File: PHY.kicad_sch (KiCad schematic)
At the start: 29 parts, among them U13 LAN8742A, Y3 25Mhz

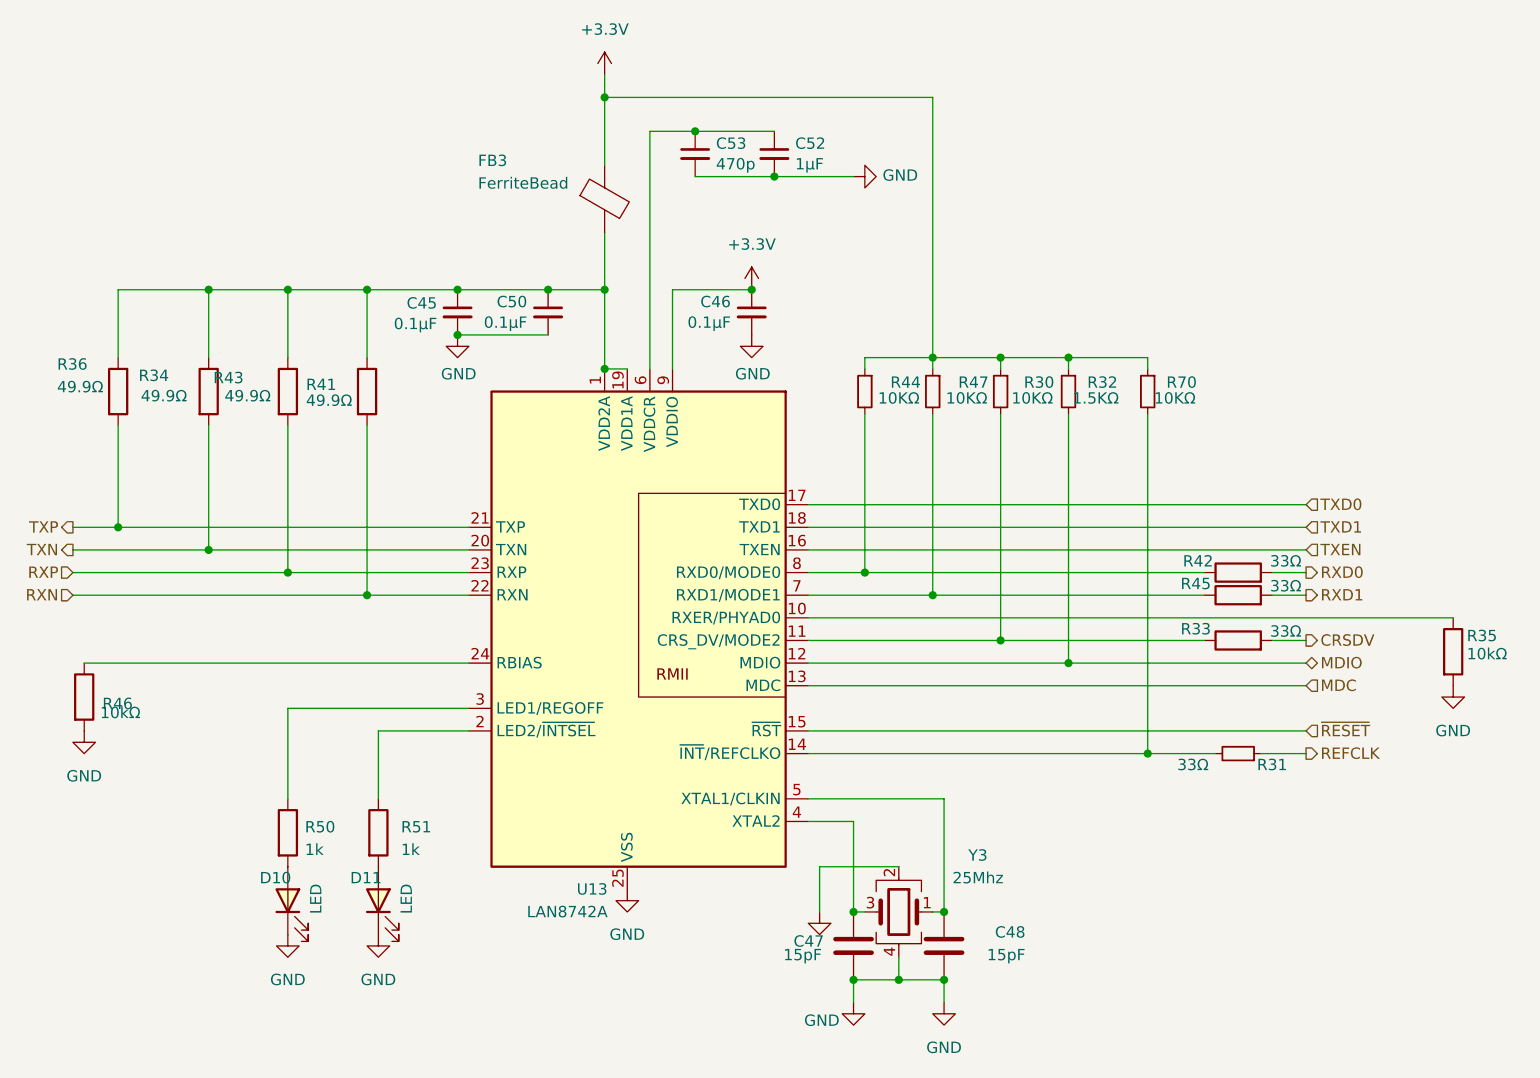
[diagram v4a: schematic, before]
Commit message: add sata capacitor
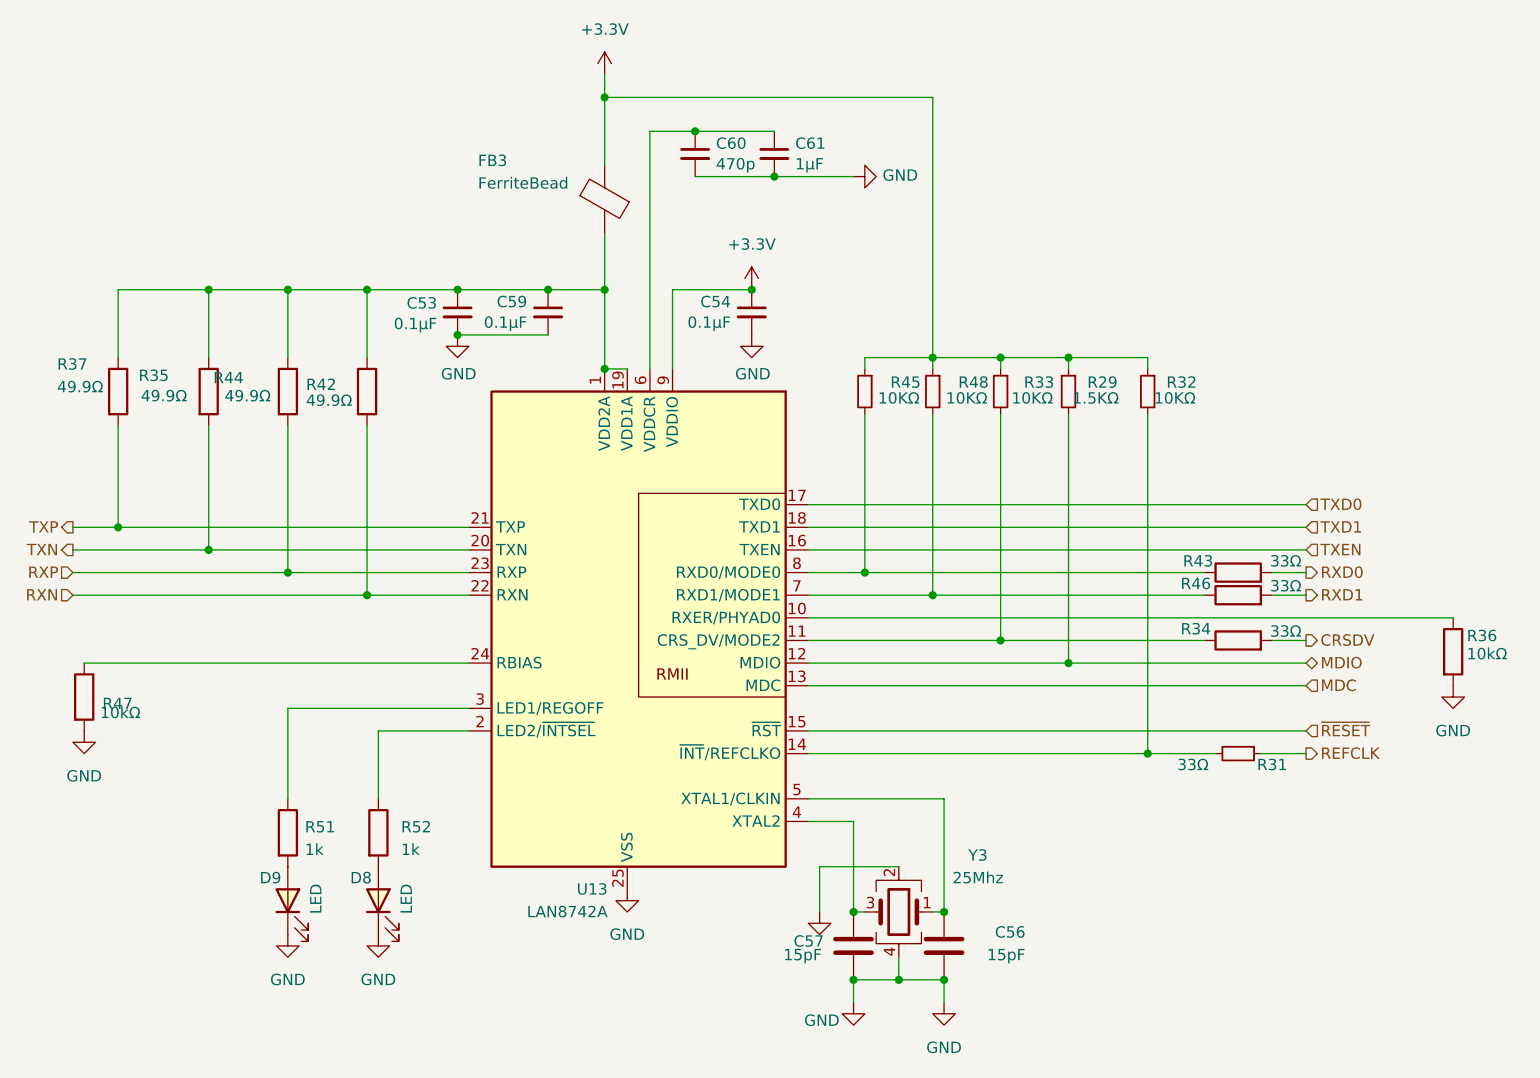
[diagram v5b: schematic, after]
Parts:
- renumbered C45 to C53, C46 to C54, C48 to C56, C47 to C57, C50 to C59, C53 to C60, C52 to C61, D11 to D8, D10 to D9, R32 to R29, R70 to R32, R30 to R33, R33 to R34, R34 to R35, R35 to R36, R36 to R37, R41 to R42, R42 to R43, R43 to R44, R44 to R45, R45 to R46, R46 to R47, R47 to R48, R50 to R51, R51 to R52
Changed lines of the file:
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@@
 		(shape input)
 		(at 78.74 116.84 180)
+		(fields_autoplaced yes)
 		(effects
 			(font
@@
 		(shape output)
 		(at 217.17 121.92 0)
+		(fields_autoplaced yes)
 		(effects
 			(font
@@
 		(shape output)
 		(at 78.74 109.22 180)
+		(fields_autoplaced yes)
 		(effects
 			(font
@@
 		(shape input)
 		(at 78.74 114.3 180)
+		(fields_autoplaced yes)
 		(effects
 			(font
@@
 		(shape output)
 		(at 217.17 134.62 0)
+		(fields_autoplaced yes)
 		(effects
 			(font
@@
 		(shape input)
 		(at 217.17 106.68 0)
+		(fields_autoplaced yes)
 		(effects
 			(font
@@
 		(shape output)
 		(at 217.17 116.84 0)
+		(fields_autoplaced yes)
 		(effects
 			(font
@@
 		(shape input)
 		(at 217.17 109.22 0)
+		(fields_autoplaced yes)
 		(effects
 			(font
@@
 		(shape input)
 		(at 217.17 127 0)
+		(fields_autoplaced yes)
 		(effects
 			(font
@@
 		(shape input)
 		(at 217.17 132.08 0)
+		(fields_autoplaced yes)
 		(effects
 			(font
@@
 		(shape output)
 		(at 217.17 114.3 0)
+		(fields_autoplaced yes)
 		(effects
 			(font
@@
 		(shape input)
 		(at 217.17 111.76 0)
+		(fields_autoplaced yes)
 		(effects
 			(font
@@
 		(shape bidirectional)
 		(at 217.17 124.46 0)
+		(fields_autoplaced yes)
 		(effects
 			(font
@@
 		(shape output)
 		(at 78.74 111.76 180)
+		(fields_autoplaced yes)
 		(effects
 			(font
@@
 		(on_board yes)
 		(dnp no)
-		(property "Reference" "R45"
+		(property "Reference" "R46"
 			(at 206.502 115.57 90)
 			(effects
@@
 			(project "mainboard4"
 				(path "/dd07ab80-a59c-44f4-ac7d-849e21e1384e/4fc6aed4-b6ec-46a7-b9d1-1f9060000df7"
-					(reference "R45")
+					(reference "R46")
 					(unit 1)
 				)
@@
 		(on_board yes)
 		(dnp no)
-		(property "Reference" "R43"
+		(property "Reference" "R44"
 			(at 94.488 92.456 0)
 			(effects
@@
 			(project "mainboard4"
 				(path "/dd07ab80-a59c-44f4-ac7d-849e21e1384e/4fc6aed4-b6ec-46a7-b9d1-1f9060000df7"
-					(reference "R43")
+					(reference "R44")
 					(unit 1)
 				)
@@
 		(on_board yes)
 		(dnp no)
-		(property "Reference" "C46"
+		(property "Reference" "C54"
 			(at 152.6032 83.9216 0)
 			(effects
@@
 			(project "mainboard4"
 				(path "/dd07ab80-a59c-44f4-ac7d-849e21e1384e/4fc6aed4-b6ec-46a7-b9d1-1f9060000df7"
-					(reference "C46")
+					(reference "C54")
 					(unit 1)
 				)
@@
 		(on_board yes)
 		(dnp no)
-		(property "Reference" "C50"
+		(property "Reference" "C59"
 			(at 129.7432 83.9216 0)
 			(effects
@@
 			(project "mainboard4"
 				(path "/dd07ab80-a59c-44f4-ac7d-849e21e1384e/4fc6aed4-b6ec-46a7-b9d1-1f9060000df7"
-					(reference "C50")
+					(reference "C59")
 					(unit 1)
 				)
@@
 		(on_board yes)
 		(dnp no)
-		(property "Reference" "D10"
+		(property "Reference" "D9"
 			(at 99.695 148.59 90)
 			(effects
@@
 			(project "mainboard4"
 				(path "/dd07ab80-a59c-44f4-ac7d-849e21e1384e/4fc6aed4-b6ec-46a7-b9d1-1f9060000df7"
-					(reference "D10")
+					(reference "D9")
 					(unit 1)
 				)
@@
 		(on_board yes)
 		(dnp no)
-		(property "Reference" "R46"
+		(property "Reference" "R47"
 			(at 82.042 129.032 0)
 			(effects
@@
 			(project "mainboard4"
 				(path "/dd07ab80-a59c-44f4-ac7d-849e21e1384e/4fc6aed4-b6ec-46a7-b9d1-1f9060000df7"
-					(reference "R46")
+					(reference "R47")
 					(unit 1)
 				)
@@
 		(on_board yes)
 		(dnp no)
-		(property "Reference" "R36"
+		(property "Reference" "R37"
 			(at 76.962 90.932 0)
 			(effects
@@
 			(project "mainboard4"
 				(path "/dd07ab80-a59c-44f4-ac7d-849e21e1384e/4fc6aed4-b6ec-46a7-b9d1-1f9060000df7"
-					(reference "R36")
+					(reference "R37")
 					(unit 1)
 				)
@@
 		(on_board yes)
 		(dnp no)
-		(property "Reference" "R42"
+		(property "Reference" "R43"
 			(at 206.756 113.03 90)
 			(effects
@@
 			(project "mainboard4"
 				(path "/dd07ab80-a59c-44f4-ac7d-849e21e1384e/4fc6aed4-b6ec-46a7-b9d1-1f9060000df7"
-					(reference "R42")
+					(reference "R43")
 					(unit 1)
 				)
@@
 		(on_board yes)
 		(dnp no)
-		(property "Reference" "R41"
+		(property "Reference" "R42"
 			(at 104.902 93.218 0)
 			(effects
@@
 			(project "mainboard4"
 				(path "/dd07ab80-a59c-44f4-ac7d-849e21e1384e/4fc6aed4-b6ec-46a7-b9d1-1f9060000df7"
-					(reference "R41")
+					(reference "R42")
 					(unit 1)
 				)
@@
 		(on_board yes)
 		(dnp no)
-		(property "Reference" "R35"
+		(property "Reference" "R36"
 			(at 235.204 121.412 0)
 			(effects
@@
 			(project "mainboard4"
 				(path "/dd07ab80-a59c-44f4-ac7d-849e21e1384e/4fc6aed4-b6ec-46a7-b9d1-1f9060000df7"
-					(reference "R35")
+					(reference "R36")
 					(unit 1)
 				)
@@
 		(on_board yes)
 		(dnp no)
-		(property "Reference" "R34"
+		(property "Reference" "R35"
 			(at 86.106 92.202 0)
 			(effects
@@
 			(project "mainboard4"
 				(path "/dd07ab80-a59c-44f4-ac7d-849e21e1384e/4fc6aed4-b6ec-46a7-b9d1-1f9060000df7"
-					(reference "R34")
+					(reference "R35")
 					(unit 1)
 				)
@@
 		(on_board yes)
 		(dnp no)
-		(property "Reference" "C52"
+		(property "Reference" "C61"
 			(at 159.8168 66.1416 0)
 			(effects
@@
 			(project "mainboard4"
 				(path "/dd07ab80-a59c-44f4-ac7d-849e21e1384e/4fc6aed4-b6ec-46a7-b9d1-1f9060000df7"
-					(reference "C52")
+					(reference "C61")
 					(unit 1)
 				)
@@
 		(on_board yes)
 		(dnp no)
-		(property "Reference" "R47"
+		(property "Reference" "R48"
 			(at 179.832 92.964 0)
 			(effects
@@
 			(project "mainboard4"
 				(path "/dd07ab80-a59c-44f4-ac7d-849e21e1384e/4fc6aed4-b6ec-46a7-b9d1-1f9060000df7"
-					(reference "R47")
+					(reference "R48")
 					(unit 1)
 				)
@@
 		(on_board yes)
 		(dnp no)
-		(property "Reference" "D11"
+		(property "Reference" "D8"
 			(at 109.855 148.59 90)
 			(effects
@@
 			(project "mainboard4"
 				(path "/dd07ab80-a59c-44f4-ac7d-849e21e1384e/4fc6aed4-b6ec-46a7-b9d1-1f9060000df7"
-					(reference "D11")
+					(reference "D8")
 					(unit 1)
 				)
@@
 		(on_board yes)
 		(dnp no)
-		(property "Reference" "C53"
+		(property "Reference" "C60"
 			(at 150.9268 66.1416 0)
 			(effects
@@
 			(project "mainboard4"
 				(path "/dd07ab80-a59c-44f4-ac7d-849e21e1384e/4fc6aed4-b6ec-46a7-b9d1-1f9060000df7"
-					(reference "C53")
+					(reference "C60")
 					(unit 1)
 				)
@@
 		(dnp no)
 		(fields_autoplaced yes)
-		(property "Reference" "R50"
+		(property "Reference" "R51"
 			(at 104.775 142.875 0)
 			(effects
@@
 			(project "mainboard4"
 				(path "/dd07ab80-a59c-44f4-ac7d-849e21e1384e/4fc6aed4-b6ec-46a7-b9d1-1f9060000df7"
-					(reference "R50")
+					(reference "R51")
 					(unit 1)
 				)
@@
 		(on_board yes)
 		(dnp no)
-		(property "Reference" "R44"
+		(property "Reference" "R45"
 			(at 172.212 92.964 0)
 			(effects
@@
 			(project "mainboard4"
 				(path "/dd07ab80-a59c-44f4-ac7d-849e21e1384e/4fc6aed4-b6ec-46a7-b9d1-1f9060000df7"
-					(reference "R44")
+					(reference "R45")
 					(unit 1)
 				)
@@
 		(on_board yes)
 		(dnp no)
-		(property "Reference" "R32"
+		(property "Reference" "R29"
 			(at 194.31 92.964 0)
 			(effects
@@
 			(project "mainboard4"
 				(path "/dd07ab80-a59c-44f4-ac7d-849e21e1384e/4fc6aed4-b6ec-46a7-b9d1-1f9060000df7"
-					(reference "R32")
+					(reference "R29")
 					(unit 1)
 				)
@@
 		(dnp no)
 		(fields_autoplaced yes)
-		(property "Reference" "R51"
+		(property "Reference" "R52"
 			(at 115.57 142.875 0)
 			(effects
@@
 			(project "mainboard4"
 				(path "/dd07ab80-a59c-44f4-ac7d-849e21e1384e/4fc6aed4-b6ec-46a7-b9d1-1f9060000df7"
-					(reference "R51")
+					(reference "R52")
 					(unit 1)
 				)
@@
 		(on_board yes)
 		(dnp no)
-		(property "Reference" "C48"
+		(property "Reference" "C56"
 			(at 185.674 154.686 0)
 			(effects
@@
 			(project "mainboard4"
 				(path "/dd07ab80-a59c-44f4-ac7d-849e21e1384e/4fc6aed4-b6ec-46a7-b9d1-1f9060000df7"
-					(reference "C48")
+					(reference "C56")
 					(unit 1)
 				)
@@
 		(on_board yes)
 		(dnp no)
-		(property "Reference" "R30"
+		(property "Reference" "R33"
 			(at 187.198 92.964 0)
 			(effects
@@
 			(project "mainboard4"
 				(path "/dd07ab80-a59c-44f4-ac7d-849e21e1384e/4fc6aed4-b6ec-46a7-b9d1-1f9060000df7"
-					(reference "R30")
+					(reference "R33")
 					(unit 1)
 				)
@@
 		(on_board yes)
 		(dnp no)
-		(property "Reference" "C45"
+		(property "Reference" "C53"
 			(at 119.634 84.074 0)
 			(effects
@@
 			(project "mainboard4"
 				(path "/dd07ab80-a59c-44f4-ac7d-849e21e1384e/4fc6aed4-b6ec-46a7-b9d1-1f9060000df7"
-					(reference "C45")
+					(reference "C53")
 					(unit 1)
 				)
@@
 		(on_board yes)
 		(dnp no)
-		(property "Reference" "C47"
+		(property "Reference" "C57"
 			(at 163.068 155.702 0)
 			(effects
@@
 			(project "mainboard4"
 				(path "/dd07ab80-a59c-44f4-ac7d-849e21e1384e/4fc6aed4-b6ec-46a7-b9d1-1f9060000df7"
-					(reference "C47")
+					(reference "C57")
 					(unit 1)
 				)
@@
 		(on_board yes)
 		(dnp no)
-		(property "Reference" "R70"
+		(property "Reference" "R32"
 			(at 203.2 92.964 0)
 			(effects
@@
 			(project "mainboard4"
 				(path "/dd07ab80-a59c-44f4-ac7d-849e21e1384e/4fc6aed4-b6ec-46a7-b9d1-1f9060000df7"
-					(reference "R70")
+					(reference "R32")
 					(unit 1)
 				)
@@
 		(on_board yes)
 		(dnp no)
-		(property "Reference" "R33"
+		(property "Reference" "R34"
 			(at 206.502 120.65 90)
 			(effects
@@
 			(project "mainboard4"
 				(path "/dd07ab80-a59c-44f4-ac7d-849e21e1384e/4fc6aed4-b6ec-46a7-b9d1-1f9060000df7"
-					(reference "R33")
+					(reference "R34")
 					(unit 1)
 				)
